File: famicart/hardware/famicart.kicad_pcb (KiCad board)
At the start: 2 copper layers, 90 x 46.1 mm, 35 parts, among them J1 Famicom 60-pin edge, U1 Raspberry Pi Pico 2, U10 74LVC1G17 (M2), U11 74LVC1G08 (/PPUACC), U12 74LVC1G07 (/IRQ), U2 74LVC541 (CPU CTRL), U3 74LVC541 (CPU A8-14), U4 74LVC541 (CPU A0-7), U5 74LVC245 (CPU D), U6 74LVC541 (PPU A8-13), U7 74LVC541 (PPU A0-7), U8 74LVC245 (PPU D), U9 74LVC139

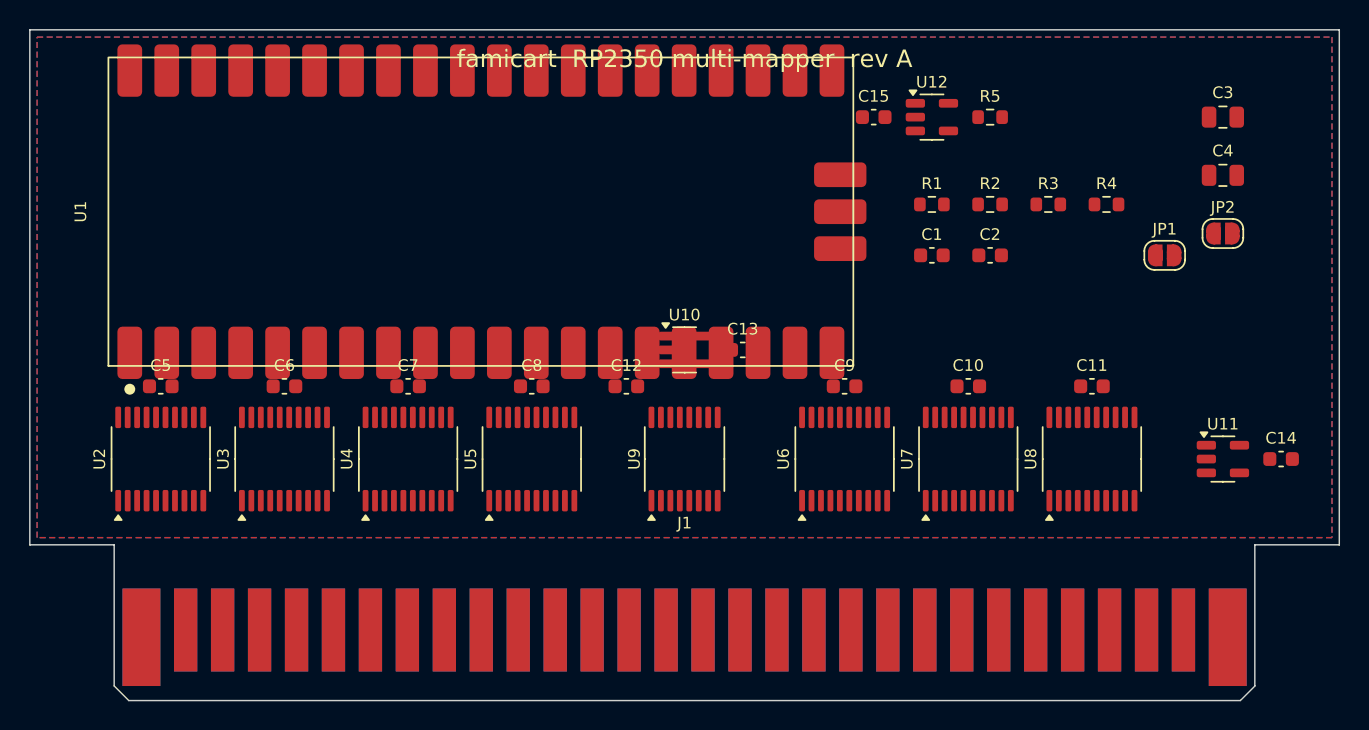
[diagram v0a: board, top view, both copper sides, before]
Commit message: famicart hardware: fully routed Famicom cartridge PCB (0 airwires, 0 DRC), fab outputs
Routing pipeline: card-edge keepout below the solder-mask line, finger pads
exposed to the router as 1 mm strips, decoupling caps moved to the back side,
0.15 mm tracks / 0.5 mm vias, Freerouting 2.0.1. Includes Gerbers, drills,
schematic/board PDFs and PNG previews, BOM and fab zip.

Co-Authored-By: Claude Fable 5.1 <noreply@anthropic.com>
Claude-Session: https://claude.ai/code/session_01RfF2rUHDV6Gz9CaznXPSPp
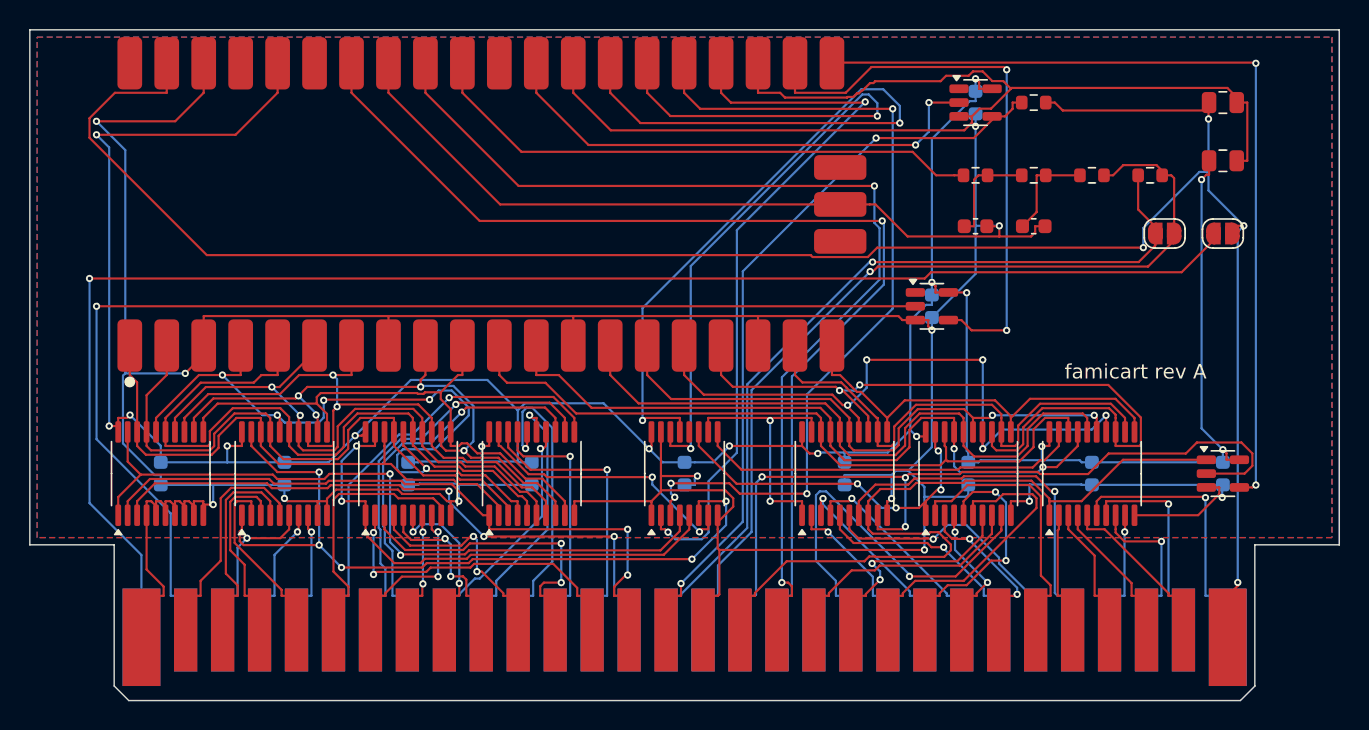
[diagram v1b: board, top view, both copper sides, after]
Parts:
- C1, C2: footprint C_0603_1608Metric -> Capacitor_SMD:C_0603_1608Metric
- C10, C11, C12, C13, C14, C15, C5, C6, C7, C8, C9: footprint C_0603_1608Metric -> Capacitor_SMD:C_0603_1608Metric; moved to B.Cu
- C3, C4: footprint C_0805_2012Metric -> Capacitor_SMD:C_0805_2012Metric
- J1: footprint Famicom_CardEdge_60 -> famicart:Famicom_CardEdge_60
- JP1, JP2: footprint SolderJumper-2_P1.3mm_Open_RoundedPad1.0x1.5mm -> Jumper:SolderJumper-2_P1.3mm_Open_RoundedPad1.0x1.5mm
- R1, R2, R3, R4, R5: footprint R_0603_1608Metric -> Resistor_SMD:R_0603_1608Metric
- U1: footprint RPi_Pico_SMD -> famicart:RPi_Pico_SMD
- U10, U11, U12: footprint SOT-23-5 -> Package_TO_SOT_SMD:SOT-23-5
- U2, U3, U4, U5, U6, U7, U8: footprint TSSOP-20_4.4x6.5mm_P0.65mm -> Package_SO:TSSOP-20_4.4x6.5mm_P0.65mm
- U9: footprint TSSOP-16_4.4x5mm_P0.65mm -> Package_SO:TSSOP-16_4.4x5mm_P0.65mm
- moved U10 17.3 mm to (62.0, 19.0)
- moved C13 13.3 mm to (62.0, 19.0), turned to -90 degrees
- moved C12 7.21 mm to (45.0, 30.5), turned to -90 degrees
- moved C15 7.07 mm to (65.0, 5.00), turned to -90 degrees
- moved C10 6.00 mm to (64.5, 30.5), turned to -90 degrees
- moved C11 6.00 mm to (73.0, 30.5), turned to -90 degrees
- moved C5 6.00 mm to (9.00, 30.5), turned to -90 degrees
- moved C6 6.00 mm to (17.5, 30.5), turned to -90 degrees
- moved C7 6.00 mm to (26.0, 30.5), turned to -90 degrees
- moved C8 6.00 mm to (34.5, 30.5), turned to -90 degrees
- moved C9 6.00 mm to (56.0, 30.5), turned to -90 degrees
- moved C14 4.12 mm to (82.0, 30.5), turned to -90 degrees
- moved C1 3.61 mm to (65.0, 13.5)
- moved C2 3.61 mm to (69.0, 13.5)
- moved R1 3.61 mm to (65.0, 10.0)
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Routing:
- net GND: track 0.00 -> 411.0 mm, vias 0 -> 13
- net +3V3: track 0.00 -> 209.7 mm, vias 0 -> 16
- net +5V: track 0.00 -> 141.0 mm, vias 0 -> 4
- net CART_PRESENT: track 0.00 -> 102.1 mm, vias 0 -> 1
- net M2: track 0.00 -> 79.3 mm, vias 0 -> 1
- net CIRAM_nCE: track 0.00 -> 71.6 mm, vias 0 -> 1
- net CIRAM_A10: track 0.00 -> 68.2 mm, vias 0 -> 2
- net SELP1: track 0.00 -> 59.7 mm, vias 0 -> 2
- net AUDIO_OUT: track 0.00 -> 59.5 mm, vias 0 -> 1
- net nPPUACC: track 0.00 -> 59.4 mm, vias 0 -> 2
- net SELC1: track 0.00 -> 57.8 mm, vias 0 -> 4
- net PPU_nWR: track 0.00 -> 55.1 mm, vias 0 -> 3
- net AUDIO_IN: track 0.00 -> 54.7 mm, vias 0 -> 1
- net PPUP5: track 0.00 -> 53.6 mm, vias 0 -> 2
- net OEC_HI: track 0.00 -> 53.1 mm, vias 0 -> 5
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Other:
- board text added: "famicart rev A"
- board text removed: "famicart RP2350 multi-mapper rev A"

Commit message: famicart rev B: USB-C port, reset switch/header, USB-CDC ROM upload; routed (0 airwires, 0 DRC)
Hardware: USB-C receptacle at the top edge wired to the Pico's USB test points
(TP2/TP3 pads per the Pico 2 datasheet, D+/D- assignment selectable by solder
jumpers, wire pads for hand assembly), CC pull-downs, RUN tactile switch and
RUN/GND header, back-side jumpers. DSN exporter fixes: unique pin ids, NPTH
keepouts, custom-pad extents, front-only placement, fixed pre-routed wires.
Firmware: USB-CDC commands INFO/RESET/BOOTSEL/LOAD/PROFILE with flash
programming of the ROM slot, host tool tools/fcload.py; TinyUSB enabled.

Co-Authored-By: Claude Fable 5.1 <noreply@anthropic.com>
Claude-Session: https://claude.ai/code/session_01RfF2rUHDV6Gz9CaznXPSPp
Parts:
- added J2: RUN/GND (console reset wire), Connector_PinHeader_2.54mm:PinHeader_1x02_P2.54mm_Vertical, F.Cu at (86.0, 20.0)
- added J3: USB-C (USB 2.0, HRO TYPE-C-31-M-12), Connector_USB:USB_C_Receptacle_HRO_TYPE-C-31-M-12, F.Cu at (76.0, 4.30)
- added JP3: USB D+ -> TP_A | TP_B, famicart:SolderJumper-3_P1.6mm_Open, B.Cu at (9.00, 6.00)
- added JP4: USB D- -> TP_B | TP_A, famicart:SolderJumper-3_P1.6mm_Open, B.Cu at (9.00, 10.0)
- added R6: 5.1k, Resistor_SMD:R_0603_1608Metric, F.Cu at (73.5, 11.5)
- added R7: 5.1k, Resistor_SMD:R_0603_1608Metric, F.Cu at (77.5, 11.5)
- added SW1: RESET (RUN), Button_Switch_SMD:SW_SPST_TL3342, F.Cu at (78.0, 21.5)
- added W1: TP wire pads (A, B, GND), famicart:WirePads_1x3, B.Cu at (9.00, 14.0)
- JP1, JP2: moved to B.Cu
- moved C15 6.58 mm to (64.0, 11.5)
- moved U12 6.58 mm to (64.0, 11.5)
- moved C3 6.50 mm to (82.0, 11.5)
- moved R5 6.50 mm to (69.0, 11.5)
- moved C4 5.50 mm to (82.0, 14.5)
- moved R1 4.50 mm to (65.0, 14.5)
- moved R2 4.50 mm to (69.0, 14.5)
- moved R3 4.50 mm to (73.0, 14.5)
- moved R4 4.50 mm to (77.0, 14.5)
- moved C1 4.00 mm to (65.0, 17.5)
- moved C2 4.00 mm to (69.0, 17.5)
- moved C13 1.50 mm to (62.0, 20.5)
- moved U10 1.50 mm to (62.0, 20.5)
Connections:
- U1 pad 30: (no net) -> RUN
- U1 pad 40: (no net) -> VBUS
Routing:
- net VBUS: track 0.00 -> 82.6 mm, vias 0 -> 3
- net USB_DM: track 0.00 -> 76.4 mm, vias 0 -> 1
- net RUN: track 0.00 -> 75.5 mm, vias 0 -> 1
- net USB_DP: track 0.00 -> 75.5 mm, vias 0 -> 1
- net CPUP2: track 52.8 -> 112.0 mm, vias 5 -> 3
- net GND: track 411.0 -> 443.7 mm, vias 13 -> 9
- net SELP1: track 59.7 -> 27.4 mm
- net +5V: track 141.0 -> 113.1 mm, vias 4 -> 2
- net OEC_LO: track 35.4 -> 62.6 mm, vias 2 -> 3
- net OEC_CTRL: track 51.0 -> 78.2 mm
- net SELP0: track 52.3 -> 28.0 mm
- net SELC1: track 57.8 -> 36.5 mm, vias 4 -> 2
- net PPUP6: track 35.4 -> 55.7 mm
- net PPU_nWR: track 55.1 -> 37.2 mm
- net USB_TPA: track 0.00 -> 16.5 mm, vias 0 -> 1
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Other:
- board text added: "FAB: 1.2 mm FR4, ENIG/hard gold fingers, 2 mm x 30 deg bevel, vias tented"
- board text added: "famicart rev B (back)"
- board text removed: "FAB: 1.2 mm FR4, ENIG/hard gold fingers, 2 mm x 30 deg bevel on card edge"
- board text removed: "famicart rev A"
- board text removed: "famicart rev A (back)"
